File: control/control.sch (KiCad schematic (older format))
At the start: 89 parts, among them M1 LMR62014, M2 LM46001, M3 STM32F4XX, M4 TPS736XX, M5 SN65HVD23X, P1 ENCODER_AB, P10 HALL_C, P2 VOLTAGE, P3 CONTROL, P4 POWER/FETS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

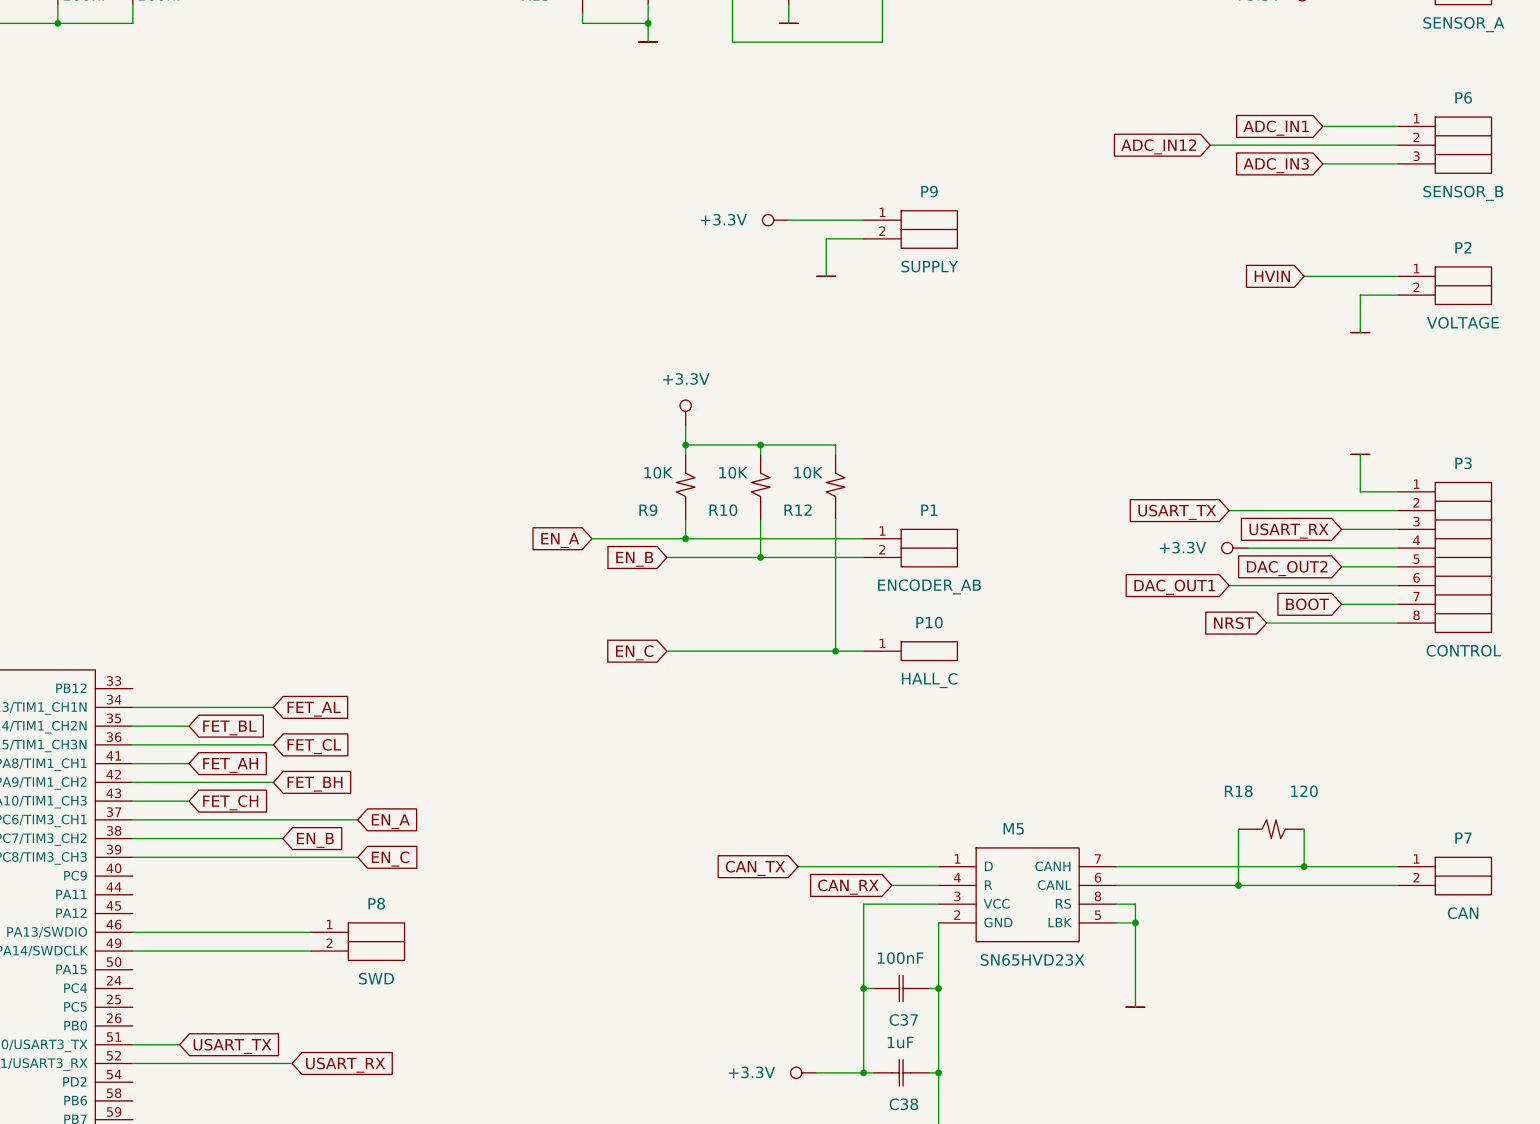
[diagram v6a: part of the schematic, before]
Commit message: Reduced decoupling capacitor bank like ESC, also added two row of pins, small fixes.
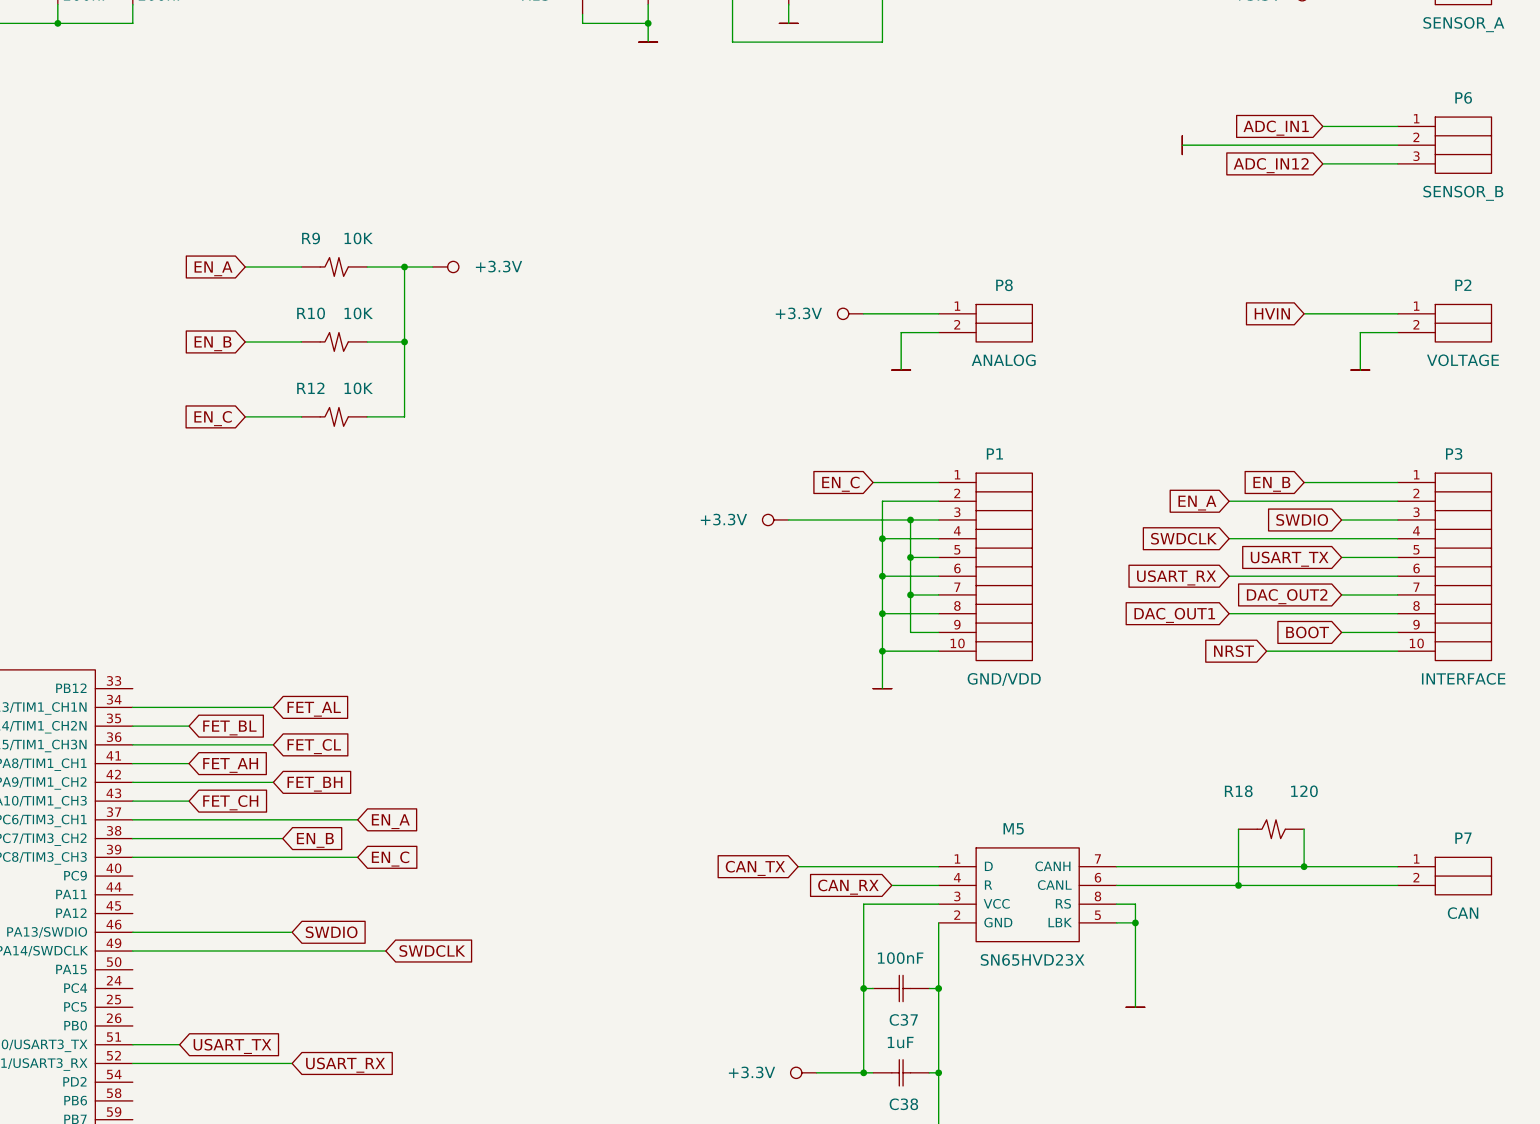
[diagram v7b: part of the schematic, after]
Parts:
- removed P1: ENCODER_AB, foot:PLS2, symbol PLS_2
- removed P10: HALL_C, foot:PLS1, symbol PLS_1
- removed P3: CONTROL, foot:PLS8, symbol PLS_8
- removed P8: SWD, foot:PLS2, symbol PLS_2
- added P1: GND/VDD, foot:PLS10, symbol PLS_10
- added P3: INTERFACE, foot:PLS10, symbol PLS_10
- P8: renamed from P9; value SUPPLY -> ANALOG
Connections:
- net +3.3V: now also P1.3, P1.5, P1.7, P1.9
- net ADC_IN12: now also P6.3; no longer P6.2
- net ADC_IN3: no longer P6.3
- net BOOT: now also P3.9
- net DAC_OUT1: now also P3.8
- net DAC_OUT2: now also P3.7
- net EN_A: now also P3.2
- net EN_B: now also P3.1
- net EN_C: now also P1.1
- net GND: now also P6.2, P1.10, P1.2, P1.4, P1.6, P1.8
- net NRST: now also P3.10
- net USART_RX: now also P3.6
- net USART_TX: now also P3.5
- net SWDIO: now reaches M3.46 (PA13/SWDIO)
- net SWDIO: now also P3.3
- net SWDCLK: now reaches M3.49 (PA14/SWDCLK)
- net SWDCLK: now also P3.4
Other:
- moved on the sheet: P2, P8, R10, R12, R9
